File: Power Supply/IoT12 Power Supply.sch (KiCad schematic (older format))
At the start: 11 parts, among them J1 Screw_Terminal_01x03, J2 Screw_Terminal_01x03

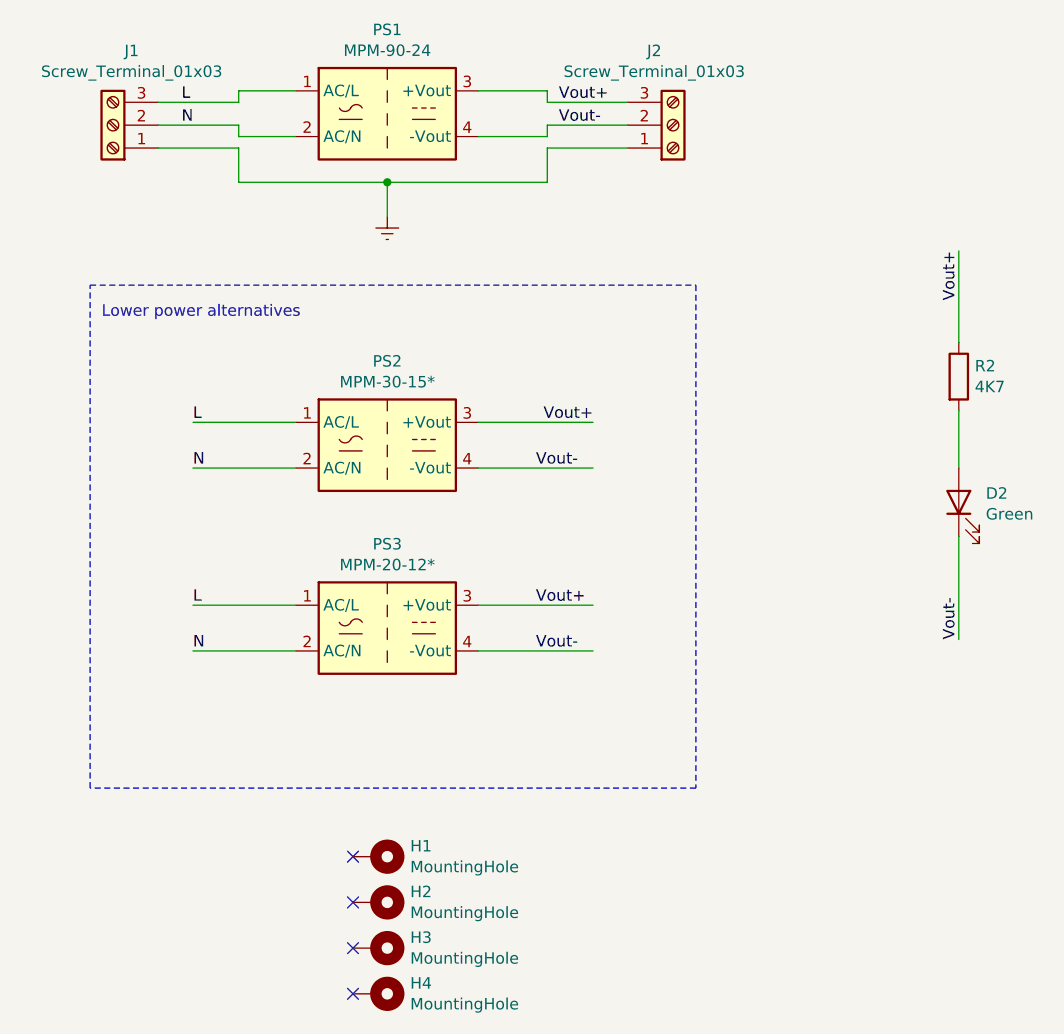
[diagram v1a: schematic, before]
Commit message: Remove all lower power supply options.
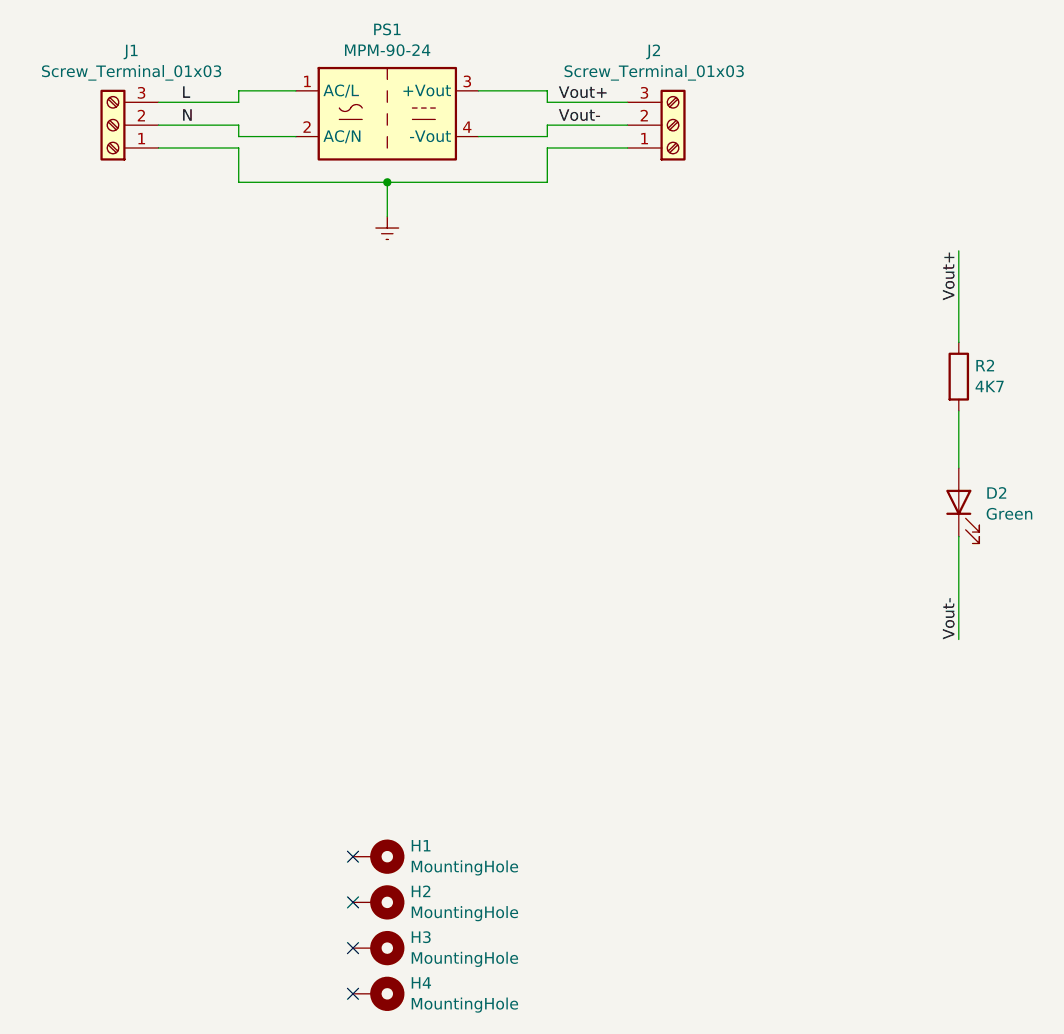
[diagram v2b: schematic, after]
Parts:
- removed PS2: MPM-30-15*, Converter-ACDC-extra:Converter_ACDC_MeanWell_MPM-30-xx_THT, symbol Converter-ACDC-extra:MPM-30-15
- removed PS3: MPM-20-12*, Converter-ACDC-extra:Converter_ACDC_MeanWell_MPM-20-xx_THT, symbol Converter-ACDC-extra:MPM-20-12
- J1, J2: footprint TerminalBlock:TerminalBlock_bornier-3_P5.08mm -> TerminalBlock-extra:TerminalBlock_Weidmueller-PM-5.08-03-90-3.5SN-BK-BX
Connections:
- wire segments 30 -> 22
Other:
- note removed: "Lower power alternatives"
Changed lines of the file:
@@
 Sheet 1 1
 Title ""
-Date "2021-10-08"
+Date "2021-10-21"
 Rev ""
 Comp "https://github.com/atoomnetmarc/IoT12-hardware"
@@
 F 0 "J1" H 4218 2125 50  0000 C CNN
 F 1 "Screw_Terminal_01x03" H 4218 2216 50  0000 C CNN
-F 2 "TerminalBlock:TerminalBlock_bornier-3_P5.08mm" H 4300 2450 50  0001 C CNN
+F 2 "TerminalBlock-extra:TerminalBlock_Weidmueller-PM-5.08-03-90-3.5SN-BK-BX" H 4300 2450 50  0001 C CNN
 F 3 "~" H 4300 2450 50  0001 C CNN
 	1    4300 2450
@@
 F 0 "J2" H 6668 2125 50  0000 C CNN
 F 1 "Screw_Terminal_01x03" H 6668 2216 50  0000 C CNN
-F 2 "TerminalBlock:TerminalBlock_bornier-3_P5.08mm" H 6750 2450 50  0001 C CNN
+F 2 "TerminalBlock-extra:TerminalBlock_Weidmueller-PM-5.08-03-90-3.5SN-BK-BX" H 6750 2450 50  0001 C CNN
 F 3 "~" H 6750 2450 50  0001 C CNN
 	1    6750 2450
@@
 	0    1    1    0
 $EndComp
-$Comp
-L Converter-ACDC-extra:MPM-30-15 PS2
-U 1 1 603A0519
-P 5500 3850
-F 0 "PS2" H 5500 4217 50  0000 C CNN
-F 1 "MPM-30-15*" H 5500 4126 50  0000 C CNN
-F 2 "Converter-ACDC-extra:Converter_ACDC_MeanWell_MPM-30-xx_THT" H 5500 3450 50  0001 C CNN
-F 3 "" H 5500 3850 50  0001 C CNN
-	1    5500 3850
-	1    0    0    -1
-$EndComp
-Wire Wire Line
-	5100 3750 4650 3750
-Wire Wire Line
-	5100 3950 4650 3950
-Wire Wire Line
-	5900 3750 6400 3750
-Wire Wire Line
-	5900 3950 6400 3950
-Text Label 4650 3750 0    50   ~ 0
-L
-Text Label 4650 3950 0    50   ~ 0
-N
 Text Label 8000 3000 3    50   ~ 0
 Vout+
-Text Label 6150 3950 0    50   ~ 0
-Vout-
-Wire Notes Line
-	4200 3150 6850 3150
-Wire Notes Line
-	6850 3150 6850 5350
-Wire Notes Line
-	6850 5350 4200 5350
-Wire Notes Line
-	4200 5350 4200 3150
-Text Notes 4250 3300 0    50   ~ 0
-Lower power alternatives
-$Comp
-L Converter-ACDC-extra:MPM-20-12 PS3
-U 1 1 603A726D
-P 5500 4650
-F 0 "PS3" H 5500 5017 50  0000 C CNN
-F 1 "MPM-20-12*" H 5500 4926 50  0000 C CNN
-F 2 "Converter-ACDC-extra:Converter_ACDC_MeanWell_MPM-20-xx_THT" H 5500 4250 50  0001 C CNN
-F 3 "" H 5500 4650 50  0001 C CNN
-	1    5500 4650
-	1    0    0    -1
-$EndComp
-Wire Wire Line
-	5100 4550 4650 4550
-Wire Wire Line
-	5100 4750 4650 4750
-Wire Wire Line
-	5900 4550 6400 4550
-Wire Wire Line
-	5900 4750 6400 4750
-Text Label 4650 4550 0    50   ~ 0
-L
-Text Label 4650 4750 0    50   ~ 0
-N
-Text Label 6150 4550 0    50   ~ 0
-Vout+
-Text Label 6150 4750 0    50   ~ 0
-Vout-
 NoConn ~ 5350 5650
 NoConn ~ 5350 5850
@@
 Wire Wire Line
 	8000 3400 8000 3000
-Text Label 6400 3750 2    50   ~ 0
-Vout+
 $EndSCHEMATC
